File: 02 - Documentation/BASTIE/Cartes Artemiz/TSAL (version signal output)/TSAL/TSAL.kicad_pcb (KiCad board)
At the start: 2 copper layers, 58 x 58 mm, 122 parts, among them J1 2P Droit 2-11-2022, J2 2P Droit 2-11-2022, J3 2P Droit 2-11-2022, J4 3P Droit 22-11-2032, J5 2P Droit 2-11-2022, J6 2P Droit 2-11-2022, J7 4P Droit 22-11-2042, J8 3P Droit 22-11-2032, J9 2P Droit 2-11-2022, Q1 NMOS SQ2348ES-T1_GE3, Q2 NMOS SQ2348ES-T1_GE3, Q3 PMOS SI2343CDS-T1-GE3, Q4 PMOS SI2343CDS-T1-GE3, U1 Opamp_Quad, U2 Opamp

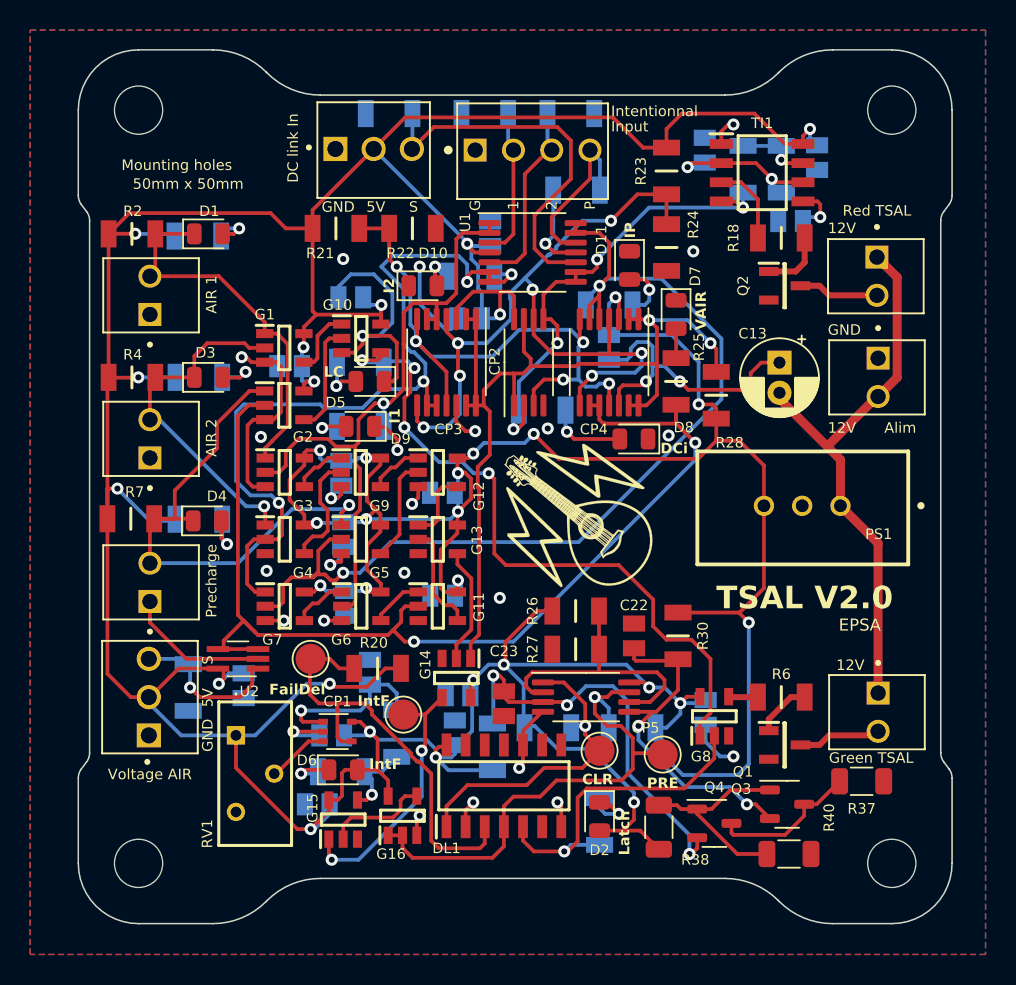
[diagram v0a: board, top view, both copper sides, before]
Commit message: Modifications cartes
Prise en compte des retours ECT + PCBs
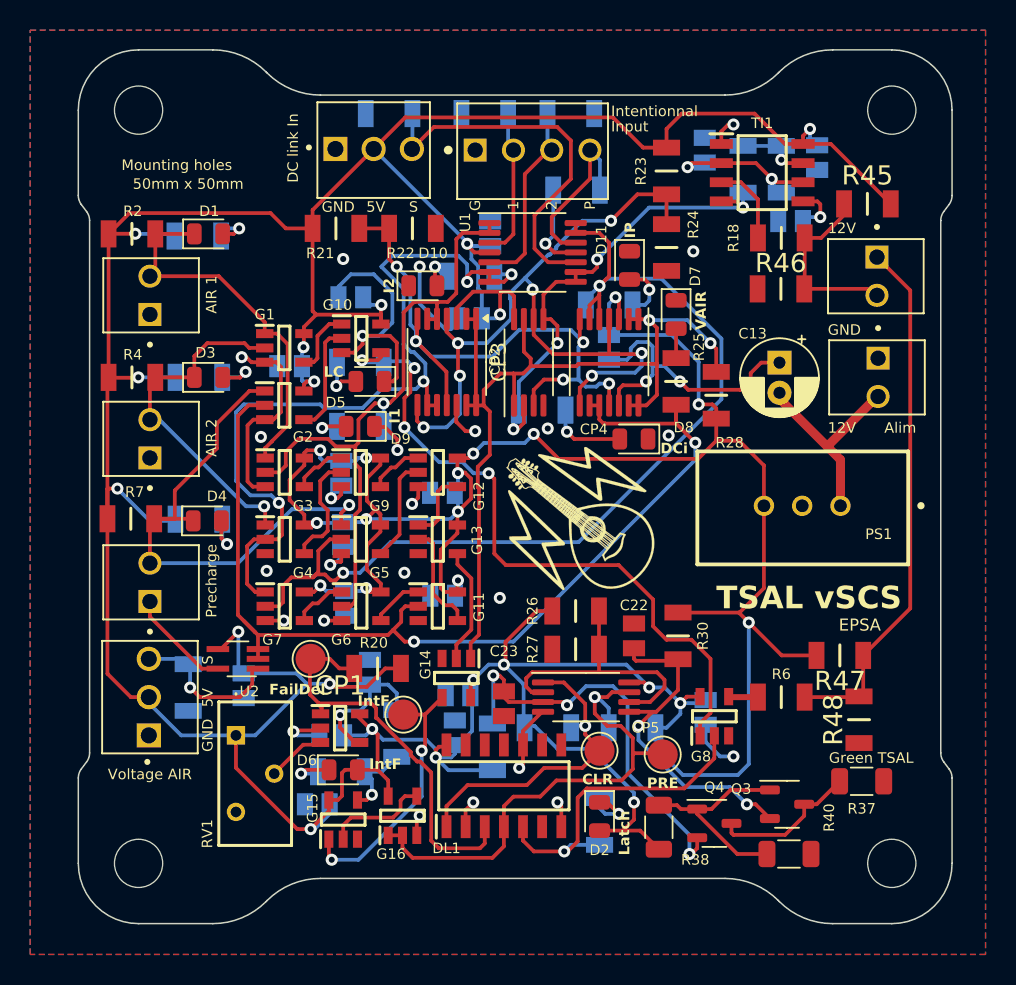
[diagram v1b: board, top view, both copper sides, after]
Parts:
- removed J5: 2P Droit 2-11-2022, EPSA:MOLEX_22-11-2022
- removed Q1, Q2: NMOS SQ2348ES-T1_GE3, EPSA:SOT95P237X112-3N
- added R45: 8k2, EPSA_lib:RESC3216X70N, F.Cu at (151.1, 36.5)
- added R46: 8k2, EPSA_lib:RESC3216X70N, F.Cu at (145.4, 42.1)
- added R47: 8k2, EPSA_lib:RESC3216X70N, F.Cu at (149.3, 66.4)
- added R48: 8k2, EPSA_lib:RESC3216X70N, F.Cu at (150.6, 70.7)
- CP1: value Comparator -> Comparateur TS391ILT; footprint Package_TO_SOT_SMD:SOT-353_SC-70-5 -> EPSA_lib:SOT95P280X145-5N
- R18, R6: value 10k -> 3k9
- moved CP1 0.29 mm to (116.1, 71.3)
- moved Ref** 0.24 mm to (132.1, 57.4)
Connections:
- C21 pad 1: Net-(CP1-+) -> Net-(CP1-IN+)
- CP1 pad 1: Net-(CP1-+) -> /Int_del
- CP1 pad 4: /Int_del -> Net-(CP1-IN+)
- J9 pad 1: +12V -> /Green_Signal_SCS
- J9 pad 2: Net-(J9-Pad2) -> /Red_Signal_SCS
- R18 pad 2: Net-(Q2-Pad1) -> /Red_Signal_SCS
- R19 pad 2: Net-(CP1-+) -> Net-(CP1-IN+)
- R6 pad 2: Net-(Q1-Pad1) -> /Green_Signal_SCS
- U2 pad 2: GND -> /VoltageAIR
- U2 pad 4: /VoltageAIR -> +5V
- U2 pad 5: +5V -> GND
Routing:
- net /Green_Signal_SCS: track 0.00 -> 35.1 mm
- net +12V: track 37.3 -> 13.5 mm
- net +5V: track 403.8 -> 417.4 mm
- net /Red_Signal_SCS: track 0.00 -> 12.4 mm
- net Net-(CP1-+): track 11.2 -> 0.00 mm, vias 1 -> 0
- net Net-(CP1-IN+): track 0.00 -> 9.03 mm, vias 0 -> 1
- net Net-(J9-Pad2): track 5.34 -> 0.00 mm
- net Net-(J5-Pad2): track 5.15 -> 0.00 mm
- net Net-(Q2-Pad1): track 4.25 -> 0.00 mm
- net Net-(Q1-Pad1): track 3.75 -> 0.00 mm
- net /VoltageAIR: track 72.1 -> 69.3 mm
- net GND: track 103.8 -> 101.7 mm
- net /Int_del: track 28.6 -> 26.6 mm
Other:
- board text added: "TSAL vSCS"
- board text removed: "Red TSAL"
- board text removed: "TSAL V2.0"

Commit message: Vérification PCBs + Fichiers Fabrication
Préparation pour production des PCBs
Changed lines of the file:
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@@
 			(drillshape 0)
 			(scaleselection 1)
-			(outputdirectory "Cirly/")
+			(outputdirectory "../../Cirly/TSAL SCS/")
 		)
 	)
@@
 			(size 1.125 1.75)
 			(layers "F.Cu" "F.Paste" "F.Mask")
-			(roundrect_rratio 0.222222)
+			(roundrect_rratio 0.2222222222)
 			(net 1 "+5V")
 			(pintype "passive")
@@
 			(size 1.125 1.75)
 			(layers "F.Cu" "F.Paste" "F.Mask")
-			(roundrect_rratio 0.222222)
+			(roundrect_rratio 0.2222222222)
 			(net 61 "Net-(Q3-Pad1)")
 			(pintype "passive")
@@
 			(size 1.125 1.75)
 			(layers "F.Cu" "F.Paste" "F.Mask")
-			(roundrect_rratio 0.222222)
+			(roundrect_rratio 0.2222222222)
 			(net 61 "Net-(Q3-Pad1)")
 			(pintype "passive")
@@
 			(size 1.125 1.75)
 			(layers "F.Cu" "F.Paste" "F.Mask")
-			(roundrect_rratio 0.222222)
+			(roundrect_rratio 0.2222222222)
 			(net 11 "GND")
 			(pintype "passive")
@@
 		(tags "Resistor")
 		(property "Reference" "R48"
-			(at -0.011901 -1.701971 270)
+			(at -0.011901 -1.701971 -90)
 			(layer "F.SilkS")
 			(effects
@@
 		)
 		(property "Value" "8k2"
-			(at 0 2.54 270)
+			(at 0 2.54 -90)
 			(layer "F.SilkS")
 			(hide yes)
@@
 		)
 		(fp_text user "${REFERENCE}"
-			(at -5.08 -2.54 270)
+			(at -5.08 -2.54 -90)
 			(layer "F.Fab")
 			(effects
@@
 		(tags "Resistor")
 		(property "Reference" "R45"
-			(at 0 -1.8796 360)
+			(at 0 -1.8796 0)
 			(layer "F.SilkS")
 			(effects
@@
 		)
 		(property "Value" "8k2"
-			(at 0 2.54 360)
+			(at 0 2.54 0)
 			(layer "F.SilkS")
 			(hide yes)
@@
 		)
 		(fp_text user "${REFERENCE}"
-			(at -5.08 -2.54 360)
+			(at -5.08 -2.54 0)
 			(layer "F.Fab")
 			(effects
@@
 			(size 1.125 1.75)
 			(layers "F.Cu" "F.Paste" "F.Mask")
-			(roundrect_rratio 0.222222)
+			(roundrect_rratio 0.2222222222)
 			(net 11 "GND")
 			(pintype "passive")
@@
 			(size 1.125 1.75)
 			(layers "F.Cu" "F.Paste" "F.Mask")
-			(roundrect_rratio 0.222222)
+			(roundrect_rratio 0.2222222222)
 			(net 62 "Net-(Q3-Pad3)")
 			(pintype "passive")
